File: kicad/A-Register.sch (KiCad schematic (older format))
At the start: 19 parts, among them U1 74LS245, U2 74LS173, U3 74LS173

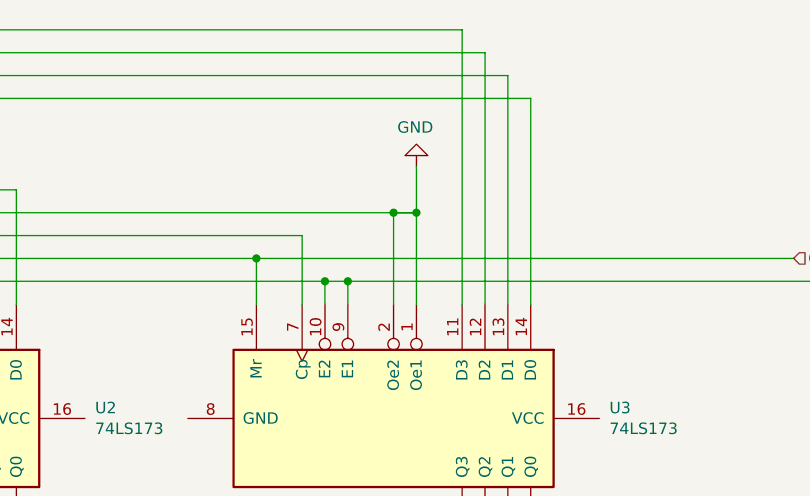
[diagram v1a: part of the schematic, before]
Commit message: Reorganize part references
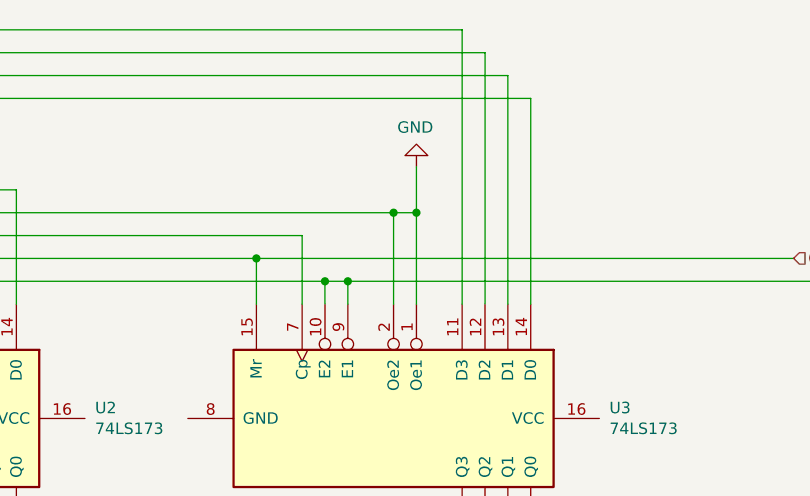
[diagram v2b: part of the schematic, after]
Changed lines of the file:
@@
 $Descr USLetter 11000 8500
 encoding utf-8
-Sheet 11 26
+Sheet 2 26
 Title "Accumulator"
 Date "2019-10-03"
@@
 	7600 1700 7600 2100
 Connection ~ 7600 1700
-Wire Wire Line
-	7600 1700 7700 1700
 $EndSCHEMATC
